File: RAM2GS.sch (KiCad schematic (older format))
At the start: 53 parts, among them J1 Memory Expansion, J2 JTAG, U1 EPM240T100, U10 74LVC1G04, U2 W9864G6KH-6, U3 60M, U4 74AHCT245, U5 74AHC245, U6 74LVT245, U7 74LVT245, U8 LD1117S33, U9 74LVC1G04

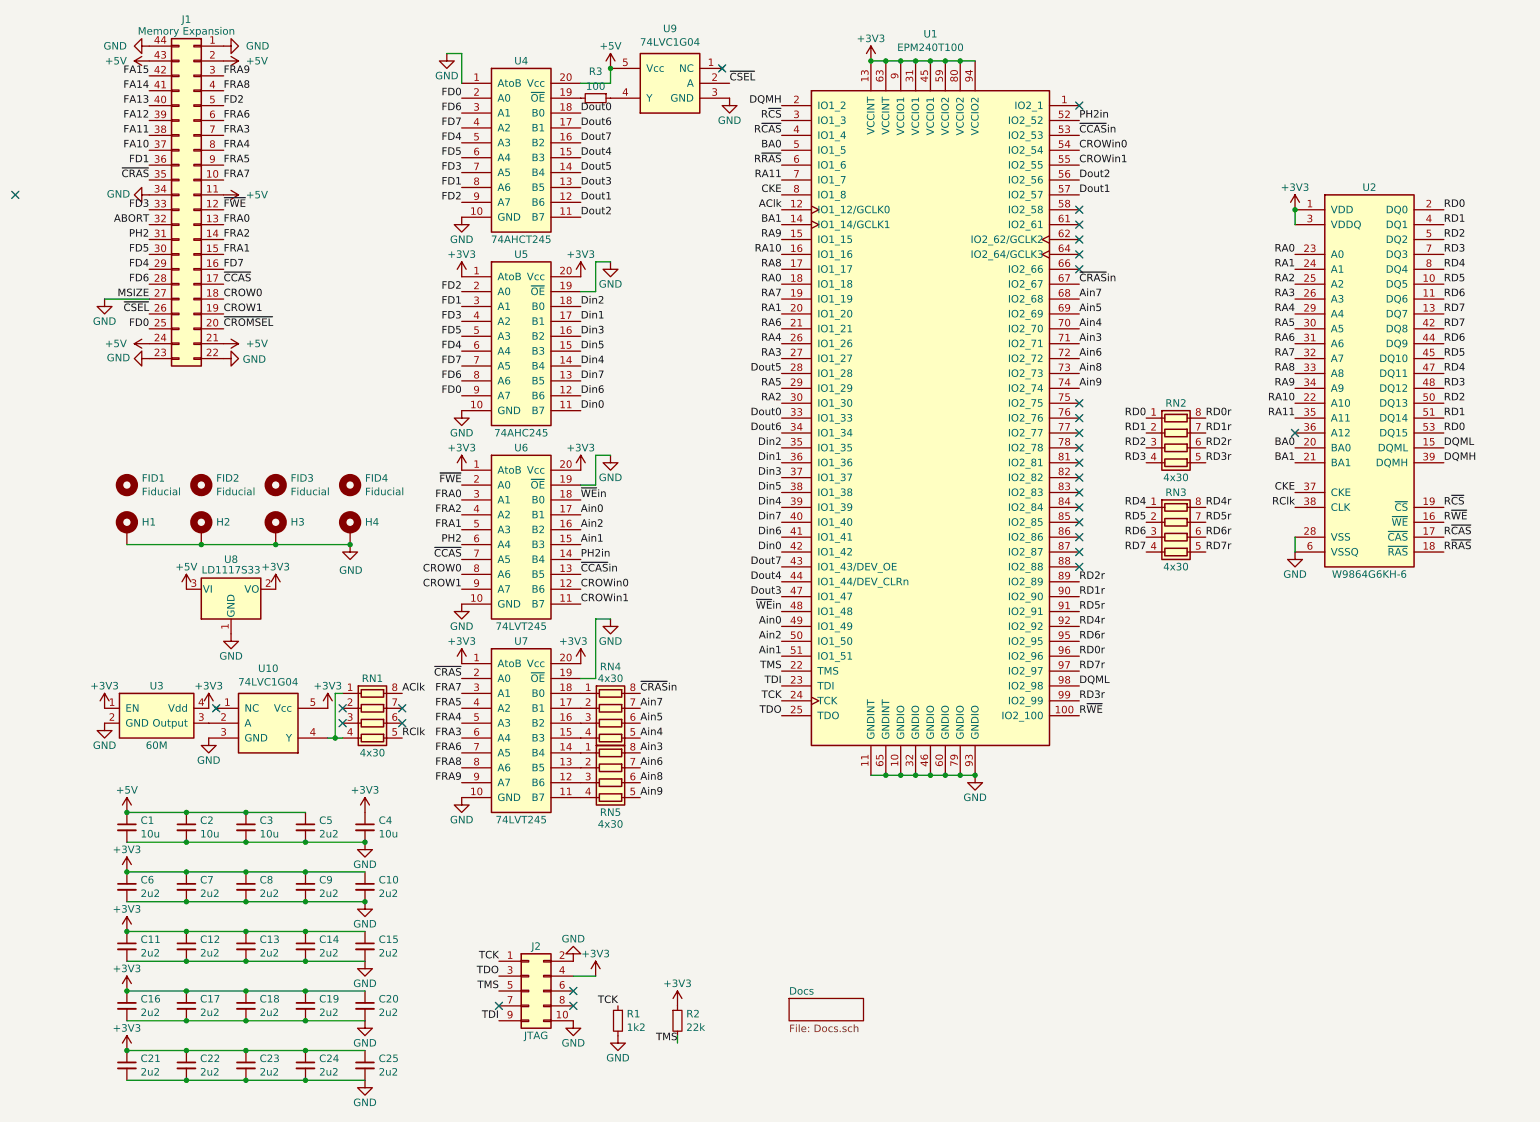
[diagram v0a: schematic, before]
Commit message: Switch to 7050 oscillator
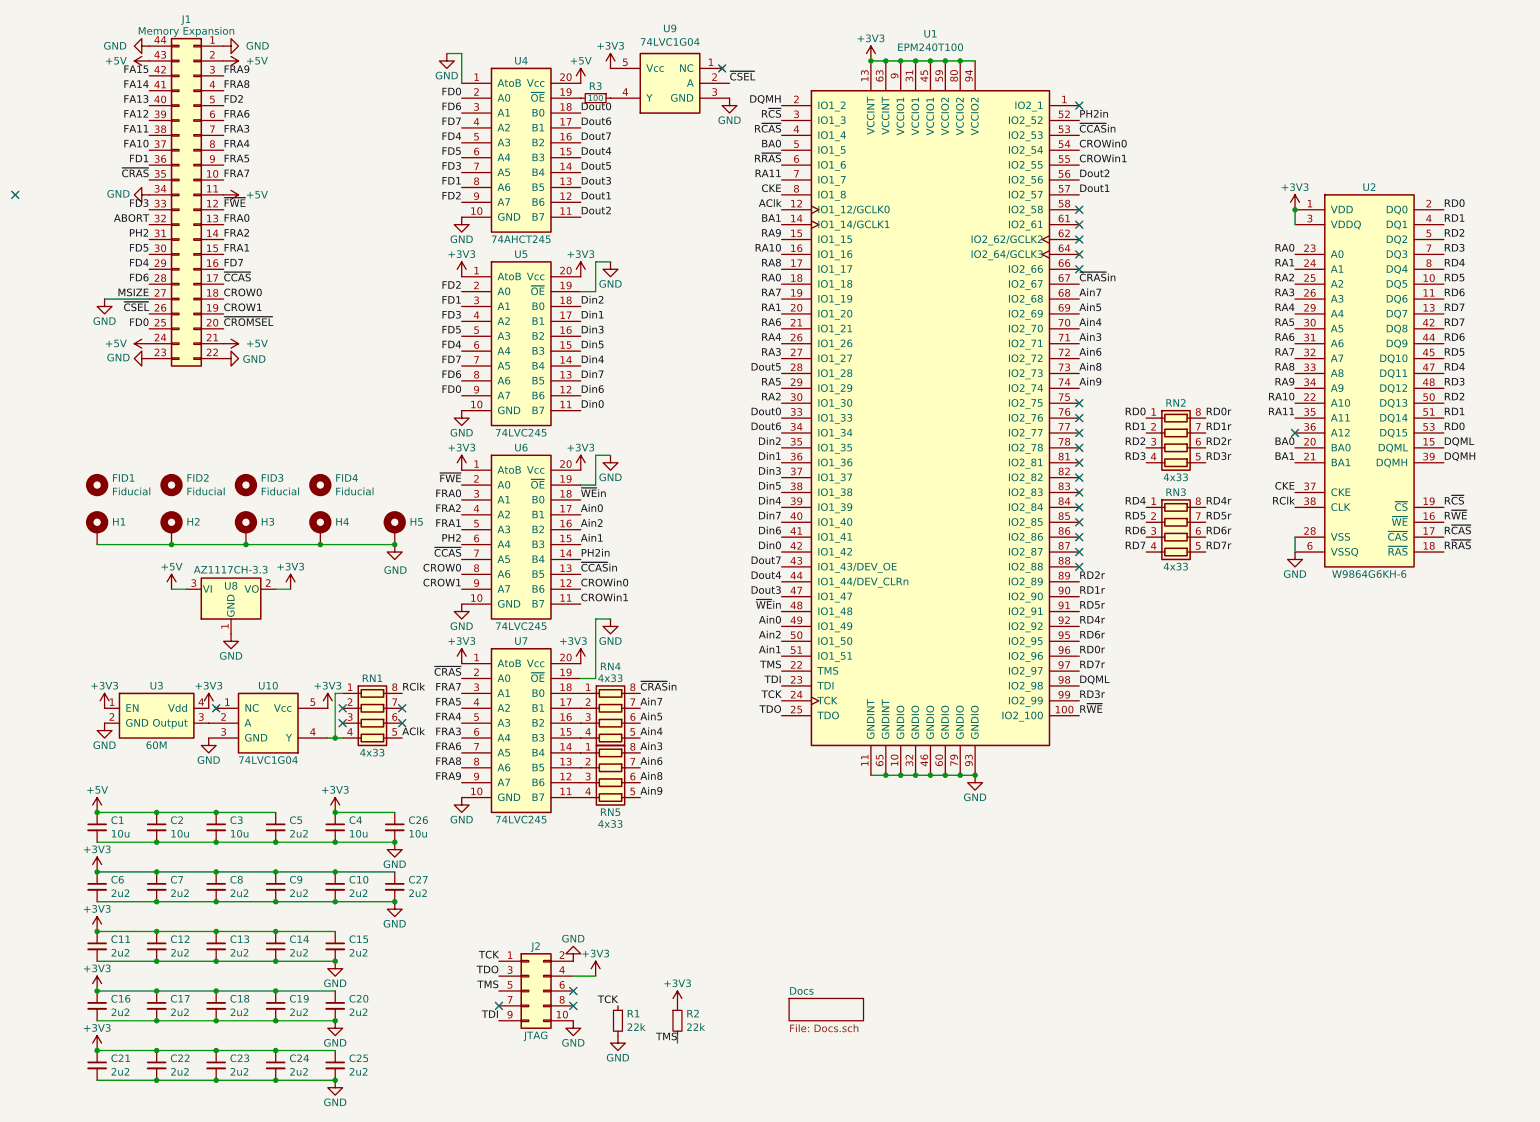
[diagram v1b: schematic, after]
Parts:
- added C26: 10u, stdpads:C_0805, symbol Device:C_Small
- added C27: 2u2, stdpads:C_0603, symbol Device:C_Small
- added H5: (no value), stdpads:PasteHole_1.152mm_NPTH, symbol Mechanical:MountingHole_Pad
- C1, C2, C3, C4: LCSC Part (none) -> C15850
- C10, C11, C12, C13, C14, C15, C16, C17, C18, C19, C20, C21, C22, C23, C24, C25, C5, C6, C7, C8, C9: LCSC Part (none) -> C23630
- H1, H2, H4: footprint stdpads:PasteHole_1.1mm_PTH -> stdpads:PasteHole_1.152mm_NPTH
- R1: value 1k2 -> 22k; LCSC Part (none) -> C17560
- R2: LCSC Part (none) -> C17560
- R3: LCSC Part (none) -> C17408
- RN1, RN2, RN3, RN4, RN5: value 4x30 -> 4x33; LCSC Part (none) -> C25501
- U1: LCSC Part (none) -> C10041
- U10, U9: LCSC Part (none) -> C10237
- U2: LCSC Part (none) -> C62379
- U3: footprint stdpads:Crystal_SMD_3225-4Pin_3.2x2.5mm -> stdpads:Crystal_SMD_7050-4Pin_7.0x5.0mm; LCSC Part (none) -> C26255
- U4: LCSC Part (none) -> C10910
- U5: value 74AHC245 -> 74LVC245; LCSC Part (none) -> C6082
- U6, U7: value 74LVT245 -> 74LVC245; LCSC Part (none) -> C6082
- U8: value LD1117S33 -> AZ1117CH-3.3; LCSC Part (none) -> C92102
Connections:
- net +3V3: now also U9.5 (Vcc), C26.1, C27.1
- net +5V: no longer U9.5 (Vcc)
- net AClk: now also RN1.5 (R4.2); no longer RN1.8 (R1.2)
- net GND: now also C26.2, C27.2, H5.1
- net RClk: now also RN1.8 (R1.2); no longer RN1.5 (R4.2)
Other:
- moved on the sheet: C1, C10, C11, C12, C13, C14, C15, C16, C17, C18, C19, C2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

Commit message: Fabbed 10/6/2020
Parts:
- RN1, RN2, RN3, RN4, RN5: footprint stdpads:Yageo_YC124 -> stdpads:R4_0402
- U1: value EPM240T100 -> EPM240T100C5N
- U10, U9: value 74LVC1G04 -> 74LVC1G04GW
- U2: value W9864G6KH-6 -> W9812G6KH-6
- U3: footprint stdpads:Crystal_SMD_7050-4Pin_7.0x5.0mm -> stdpads:Crystal_SMD_7050-4Pin_7.0x5.0mm_SiTime
- U4: value 74AHCT245 -> 74AHCT245PW; LCSC Part C10910 -> C173388
- U5, U6, U7: value 74LVC245 -> 74LVC245APW
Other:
- moved on the sheet: J2, R1, R2, RN1, U10, U3

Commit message: Fabbed
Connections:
- net GND: now also U2.36 (A12)
- no-connect marks 29 -> 28
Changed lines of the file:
@@
 Sheet 1 2
 Title "GW4201D (RAM2GS II)"
-Date "2020-09-29"
-Rev "1.1"
+Date "2021-03-02"
+Rev "1.2"
 Comp "Garrett's Workshop"
 Comment1 ""
@@
 	-1   0    0    -1
 $EndComp
-Wire Wire Line
-	8700 4200 8700 4100
 $Comp
 L power:+3V3 #PWR0131
@@
 Text Label 4900 1050 0    50   ~ 0
 ~CSEL~
-NoConn ~ 8700 3400
 $Comp
 L Mechanical:MountingHole_Pad H5
@@
 	1    0    0    -1
 $EndComp
+Wire Wire Line
+	8700 4200 8700 4100
+Connection ~ 8700 4200
+$Comp
+L power:GND #PWR?
+U 1 1 607C165A
+P 8700 3400
+F 0 "#PWR?" H 8700 3150 50  0001 C CNN
+F 1 "GND" H 8700 3250 50  0000 C CNN
+F 2 "" H 8700 3400 50  0001 C CNN
+F 3 "" H 8700 3400 50  0001 C CNN
+	1    8700 3400
+	0    1    -1   0
+$EndComp
 $EndSCHEMATC

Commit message: Added 1.8V regulator
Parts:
- added C28: 2u2, stdpads:C_0603, symbol Device:C_Small
- added R4: 0, stdpads:R_0805, symbol Device:R_Small
- added U11: DNP, stdpads:SOT-23-5, symbol Regulator_Linear:AP2127K-1.8
- U1: symbol GW_PLD:EPM240T100 -> GW_PLD:5M240ZT100
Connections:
- net +3V3: now also R4.1; no longer C14.1, C9.1, U1.13 (VCCINT), U1.63 (VCCINT)
- net +5V: now also U11.1 (VIN), U11.3 (EN)
- net GND: now also U1.1 (GND), C28.2, U11.2 (GND)
- new net +1V8: C14.1, C28.1, C9.1, R4.2, U1.13 (VCCINT), U1.63 (VCCINT), U11.5 (VOUT)
- no-connect marks 28 -> 27
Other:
- moved on the sheet: C10, C14, C27, C9
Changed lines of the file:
@@
 encoding utf-8
 Sheet 1 2
-Title "GW4201D (RAM2GS II)"
-Date "2021-03-02"
-Rev "1.2"
+Title "GW4201D (RAM2GS II) - EPM240 / 5M240Z / AG256"
+Date "2021-04-29"
+Rev "2.0"
 Comp "Garrett's Workshop"
 Comment1 ""
@@
 L power:+3V3 #PWR0133
 U 1 1 5E9850F8
-P 1950 4450
-F 0 "#PWR0133" H 1950 4300 50  0001 C CNN
-F 1 "+3V3" H 1950 4600 50  0000 C CNN
-F 2 "" H 1950 4450 50  0001 C CNN
-F 3 "" H 1950 4450 50  0001 C CNN
-	1    1950 4450
+P 2050 4450
+F 0 "#PWR0133" H 2050 4300 50  0001 C CNN
+F 1 "+3V3" H 2050 4600 50  0000 C CNN
+F 2 "" H 2050 4450 50  0001 C CNN
+F 3 "" H 2050 4450 50  0001 C CNN
+	1    2050 4450
 	1    0    0    -1
 $EndComp
@@
 Connection ~ 8700 1900
 $Comp
-L GW_PLD:EPM240T100 U1
+L GW_PLD:5M240ZT100 U1
 U 1 1 5E9D5897
 P 6250 3300
-F 0 "U1" H 6250 5881 50  0000 C CNN
-F 1 "EPM240T100C5N" H 6250 5790 50  0000 C CNN
+F 0 "U1" H 6200 5850 50  0000 C CNN
+F 1 "EPM240T100C5N" H 6200 5750 50  0000 C CNN
 F 2 "stdpads:TQFP-100_14x14mm_P0.5mm" H 6250 3200 20  0001 C CNN
 F 3 "https://www.altera.com/content/dam/altera-www/global/en_US/pdfs/literature/hb/max2/max2_mii5v1.pdf" H 6250 3300 50  0001 C CNN
@@
 L power:+3V3 #PWR0135
 U 1 1 5E9DE55C
-P 5850 900
-F 0 "#PWR0135" H 5850 750 50  0001 C CNN
-F 1 "+3V3" H 5850 1050 50  0000 C CNN
-F 2 "" H 5850 900 50  0001 C CNN
-F 3 "" H 5850 900 50  0001 C CNN
-	1    5850 900
+P 6550 900
+F 0 "#PWR0135" H 6550 750 50  0001 C CNN
+F 1 "+3V3" H 6550 1050 50  0000 C CNN
+F 2 "" H 6550 900 50  0001 C CNN
+F 3 "" H 6550 900 50  0001 C CNN
+	1    6550 900
 	1    0    0    -1
 $EndComp
@@
 L power:GND #PWR0136
 U 1 1 5E9DF65F
-P 6550 5700
-F 0 "#PWR0136" H 6550 5450 50  0001 C CNN
-F 1 "GND" H 6550 5550 50  0000 C CNN
-F 2 "" H 6550 5700 50  0001 C CNN
-F 3 "" H 6550 5700 50  0001 C CNN
-	1    6550 5700
+P 6650 5700
+F 0 "#PWR0136" H 6650 5450 50  0001 C CNN
+F 1 "GND" H 6650 5550 50  0000 C CNN
+F 2 "" H 6650 5700 50  0001 C CNN
+F 3 "" H 6650 5700 50  0001 C CNN
+	1    6650 5700
 	-1   0    0    -1
 $EndComp
@@
 $EndComp
 Wire Wire Line
-	1850 6950 2250 6950
-Connection ~ 1850 6950
-Wire Wire Line
-	1850 6750 2250 6750
-Connection ~ 1850 6750
-$Comp
-L Device:C_Small C14
-U 1 1 5F25E505
-P 1850 6850
-F 0 "C14" H 1942 6896 50  0000 L CNN
-F 1 "2u2" H 1942 6805 50  0000 L CNN
-F 2 "stdpads:C_0603" H 1850 6850 50  0001 C CNN
-F 3 "~" H 1850 6850 50  0001 C CNN
-F 4 "C23630" H 1850 6850 50  0001 C CNN "LCSC Part"
-	1    1850 6850
-	1    0    0    -1
-$EndComp
-Wire Wire Line
-	1450 6950 1850 6950
-Wire Wire Line
 	1050 6950 1450 6950
 Connection ~ 1450 6950
-Wire Wire Line
-	1450 6750 1850 6750
 Wire Wire Line
 	1050 6750 1450 6750
@@
 $EndComp
 $Comp
-L Device:C_Small C10
-U 1 1 5F25BCF6
+L Device:C_Small C9
+U 1 1 5F2596EA
 P 2250 6450
-F 0 "C10" H 2342 6496 50  0000 L CNN
+F 0 "C9" H 2342 6496 50  0000 L CNN
 F 1 "2u2" H 2342 6405 50  0000 L CNN
 F 2 "stdpads:C_0603" H 2250 6450 50  0001 C CNN
@@
 F 4 "C23630" H 2250 6450 50  0001 C CNN "LCSC Part"
 	1    2250 6450
-	1    0    0    -1
-$EndComp
-Wire Wire Line
-	1850 6550 2250 6550
-Wire Wire Line
-	1450 6550 1850 6550
-Connection ~ 1850 6550
-Wire Wire Line
-	1850 6350 2250 6350
-Wire Wire Line
-	1450 6350 1850 6350
-Connection ~ 1850 6350
-$Comp
-L Device:C_Small C9
-U 1 1 5F2596EA
-P 1850 6450
-F 0 "C9" H 1942 6496 50  0000 L CNN
-F 1 "2u2" H 1942 6405 50  0000 L CNN
-F 2 "stdpads:C_0603" H 1850 6450 50  0001 C CNN
-F 3 "~" H 1850 6450 50  0001 C CNN
-F 4 "C23630" H 1850 6450 50  0001 C CNN "LCSC Part"
-	1    1850 6450
 	1    0    0    -1
 $EndComp
@@
 	1    650  6750
 	1    0    0    -1
-$EndComp
-Connection ~ 2250 6550
-$Comp
-L power:GND #PWR0140
-U 1 1 5F21322E
-P 2650 6550
-F 0 "#PWR0140" H 2650 6300 50  0001 C CNN
-F 1 "GND" H 2650 6400 50  0000 C CNN
-F 2 "" H 2650 6550 50  0001 C CNN
-F 3 "" H 2650 6550 50  0001 C CNN
-	1    2650 6550
-	-1   0    0    -1
 $EndComp
 Connection ~ 650  6350
@@
 	1    0    0    -1
 $EndComp
-NoConn ~ 7250 1200
 Wire Wire Line
 	5850 900  5950 900
 Wire Wire Line
 	5850 5700 5950 5700
-Connection ~ 5850 900
-Connection ~ 5950 900
-Wire Wire Line
-	5950 900  6050 900
-Connection ~ 6050 900
 Wire Wire Line
 	6050 900  6150 900
@@
 $EndComp
 Wire Wire Line
-	1950 4450 1850 4450
+	2050 4450 1850 4450
 Wire Wire Line
 	1150 4450 1250 4450
@@
 $EndComp
 $Comp
-L Device:C_Small C27
-U 1 1 5F944E67
-P 2650 6450
-F 0 "C27" H 2742 6496 50  0000 L CNN
-F 1 "2u2" H 2742 6405 50  0000 L CNN
-F 2 "stdpads:C_0603" H 2650 6450 50  0001 C CNN
-F 3 "~" H 2650 6450 50  0001 C CNN
-F 4 "C23630" H 2650 6450 50  0001 C CNN "LCSC Part"
-	1    2650 6450
-	1    0    0    -1
-$EndComp
-Wire Wire Line
-	2650 6350 2250 6350
-Connection ~ 2250 6350
-Wire Wire Line
-	2250 6550 2650 6550
-Connection ~ 2650 6550
-$Comp
 L GW_Logic:74245 U4
 U 1 1 5E950437
@@
 Connection ~ 8700 4200
 $Comp
-L power:GND #PWR?
+L power:GND #PWR0158
 U 1 1 607C165A
 P 8700 3400
-F 0 "#PWR?" H 8700 3150 50  0001 C CNN
+F 0 "#PWR0158" H 8700 3150 50  0001 C CNN
 F 1 "GND" H 8700 3250 50  0000 C CNN
 F 2 "" H 8700 3400 50  0001 C CNN
@@
 	0    1    -1   0
 $EndComp
+$Comp
+L power:GND #PWR0159
+U 1 1 871A171C
+P 1550 5550
+F 0 "#PWR0159" H 1550 5300 50  0001 C CNN
+F 1 "GND" H 1550 5400 50  0000 C CNN
+F 2 "" H 1550 5550 50  0001 C CNN
+F 3 "" H 1550 5550 50  0001 C CNN
+	1    1550 5550
+	-1   0    0    -1
+$EndComp
+Wire Wire Line
+	1250 5250 1150 5250
+Wire Wire Line
+	1150 5250 1150 5150
+Connection ~ 1150 4450
+Wire Wire Line
+	1250 5150 1150 5150
+Connection ~ 1150 5150
+Wire Wire Line
+	1150 5150 1150 4450
+$Comp
+L Regulator_Linear:AP2127K-1.8 U11
+U 1 1 8719FB68
+P 1550 5250
+F 0 "U11" H 1550 5250 50  0000 C CNN
+F 1 "DNP" H 1550 5450 50  0000 C BNN
+F 2 "stdpads:SOT-23-5" H 1550 5575 50  0001 C CNN
+F 3 "https://www.diodes.com/assets/Datasheets/AP2127.pdf" H 1550 5350 50  0001 C CNN
+	1    1550 5250
+	1    0    0    -1
+$EndComp
+Wire Wire Line
+	1850 5150 2050 5150
+$Comp
+L Device:C_Small C28
+U 1 1 871B6E7B
+P 2050 5250
+F 0 "C28" H 2142 5296 50  0000 L CNN
+F 1 "2u2" H 2142 5205 50  0000 L CNN
+F 2 "stdpads:C_0603" H 2050 5250 50  0001 C CNN
+F 3 "~" H 2050 5250 50  0001 C CNN
+F 4 "C23630" H 2050 5250 50  0001 C CNN "LCSC Part"
+	1    2050 5250
+	1    0    0    -1
+$EndComp
+Wire Wire Line
+	2050 5350 2050 5550
+Wire Wire Line
+	2050 5550 1550 5550
+Connection ~ 1550 5550
+$Comp
+L power:+1V8 #PWR0160
+U 1 1 871BC45D
+P 2050 5150
+F 0 "#PWR0160" H 2050 5000 50  0001 C CNN
+F 1 "+1V8" H 2050 5300 50  0000 C CNN
+F 2 "" H 2050 5150 50  0001 C CNN
+F 3 "" H 2050 5150 50  0001 C CNN
+	1    2050 5150
+	1    0    0    -1
+$EndComp
+Connection ~ 2050 5150
+$Comp
+L Device:R_Small R4
+U 1 1 871C5B73
+P 1850 4800
+F 0 "R4" H 1791 4846 50  0000 R CNN
+F 1 "0" H 1791 4755 50  0000 R CNN
+F 2 "stdpads:R_0805" H 1850 4800 50  0001 C CNN
+F 3 "~" H 1850 4800 50  0001 C CNN
+F 4 "C17477" H 1850 4800 50  0001 C CNN "LCSC Part"
+	1    1850 4800
+	-1   0    0    -1
+$EndComp
+Wire Wire Line
+	1850 4700 1850 4450
+Connection ~ 1850 4450
+Connection ~ 1850 5150
+Wire Wire Line
+	1850 4900 1850 5150
+Wire Wire Line
+	6650 5700 6550 5700
+Connection ~ 6650 5700
+Connection ~ 6550 900
+$Comp
+L power:+1V8 #PWR?
+U 1 1 871E812C
+P 5850 900
+F 0 "#PWR?" H 5850 750 50  0001 C CNN
+F 1 "+1V8" H 5850 1050 50  0000 C CNN
+F 2 "" H 5850 900 50  0001 C CNN
+F 3 "" H 5850 900 50  0001 C CNN
+	1    5850 900
+	1    0    0    -1
+$EndComp
+Connection ~ 5850 900
+$Comp
+L power:GND #PWR0140
+U 1 1 5F21322E
+P 2650 6550
+F 0 "#PWR0140" H 2650 6300 50  0001 C CNN
+F 1 "GND" H 2650 6400 50  0000 C CNN
+F 2 "" H 2650 6550 50  0001 C CNN
+F 3 "" H 2650 6550 50  0001 C CNN
+	1    2650 6550
+	-1   0    0    -1
+$EndComp
+$Comp
+L Device:C_Small C27
+U 1 1 5F944E67
+P 1850 6450
+F 0 "C27" H 1942 6496 50  0000 L CNN
+F 1 "2u2" H 1942 6405 50  0000 L CNN
+F 2 "stdpads:C_0603" H 1850 6450 50  0001 C CNN
+F 3 "~" H 1850 6450 50  0001 C CNN
+F 4 "C23630" H 1850 6450 50  0001 C CNN "LCSC Part"
+	1    1850 6450
+	1    0    0    -1
+$EndComp
+$Comp
+L Device:C_Small C14
+U 1 1 5F25E505
+P 2650 6450
+F 0 "C14" H 2742 6496 50  0000 L CNN
+F 1 "2u2" H 2742 6405 50  0000 L CNN
+F 2 "stdpads:C_0603" H 2650 6450 50  0001 C CNN
+F 3 "~" H 2650 6450 50  0001 C CNN
+F 4 "C23630" H 2650 6450 50  0001 C CNN "LCSC Part"
+	1    2650 6450
+	1    0    0    -1
+$EndComp
+Connection ~ 1850 6750
+Wire Wire Line
+	1850 6750 2250 6750
+Connection ~ 1850 6950
+Wire Wire Line
+	1850 6950 2250 6950
+Wire Wire Line
+	1450 6550 1850 6550
+Wire Wire Line
+	1450 6350 1850 6350
+Wire Wire Line
+	1450 6950 1850 6950
+Wire Wire Line
+	1450 6750 1850 6750
+$Comp
+L Device:C_Small C10
+U 1 1 5F25BCF6
+P 1850 6850
+F 0 "C10" H 1942 6896 50  0000 L CNN
+F 1 "2u2" H 1942 6805 50  0000 L CNN
+F 2 "stdpads:C_0603" H 1850 6850 50  0001 C CNN
+F 3 "~" H 1850 6850 50  0001 C CNN
+F 4 "C23630" H 1850 6850 50  0001 C CNN "LCSC Part"
+	1    1850 6850
+	1    0    0    -1
+$EndComp
+Connection ~ 1850 6550
+Wire Wire Line
+	1850 6550 2250 6550
+Wire Wire Line
+	2250 6350 2650 6350
+Connection ~ 2250 6550
+Wire Wire Line
+	2250 6550 2650 6550
+Connection ~ 2650 6550
+$Comp
+L power:+1V8 #PWR?
+U 1 1 87222813
+P 2250 6350
+F 0 "#PWR?" H 2250 6200 50  0001 C CNN
+F 1 "+1V8" H 2250 6500 50  0000 C CNN
+F 2 "" H 2250 6350 50  0001 C CNN
+F 3 "" H 2250 6350 50  0001 C CNN
+	1    2250 6350
+	1    0    0    -1
+$EndComp
+Connection ~ 2250 6350
 $EndSCHEMATC
